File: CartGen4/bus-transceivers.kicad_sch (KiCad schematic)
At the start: 5 parts

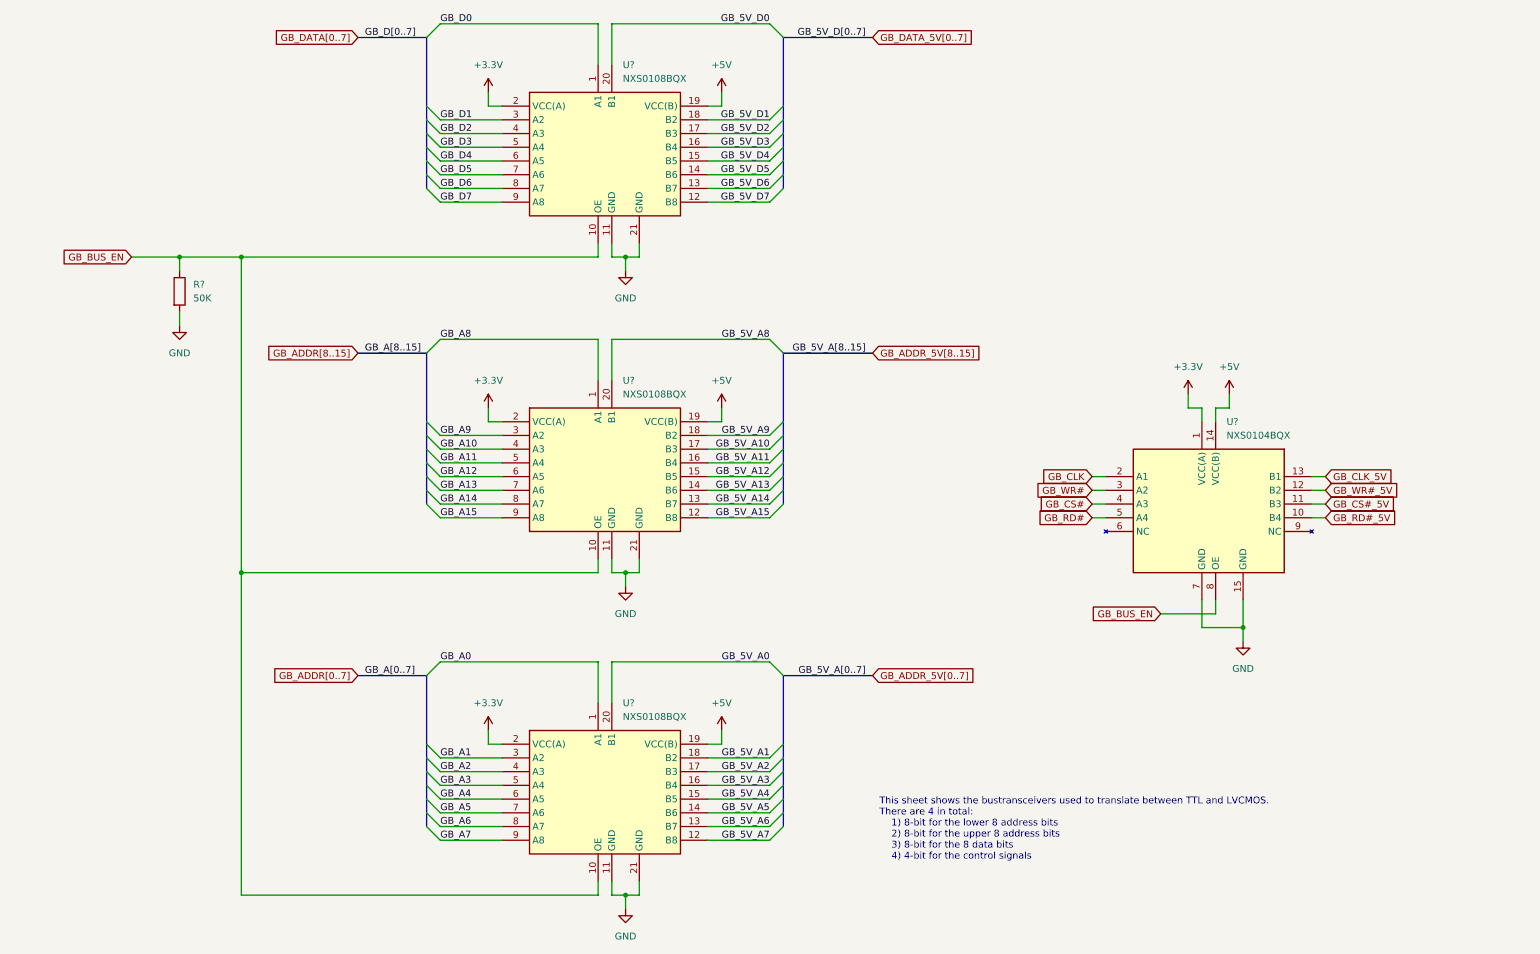
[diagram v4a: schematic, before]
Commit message: Added reference designators to everything
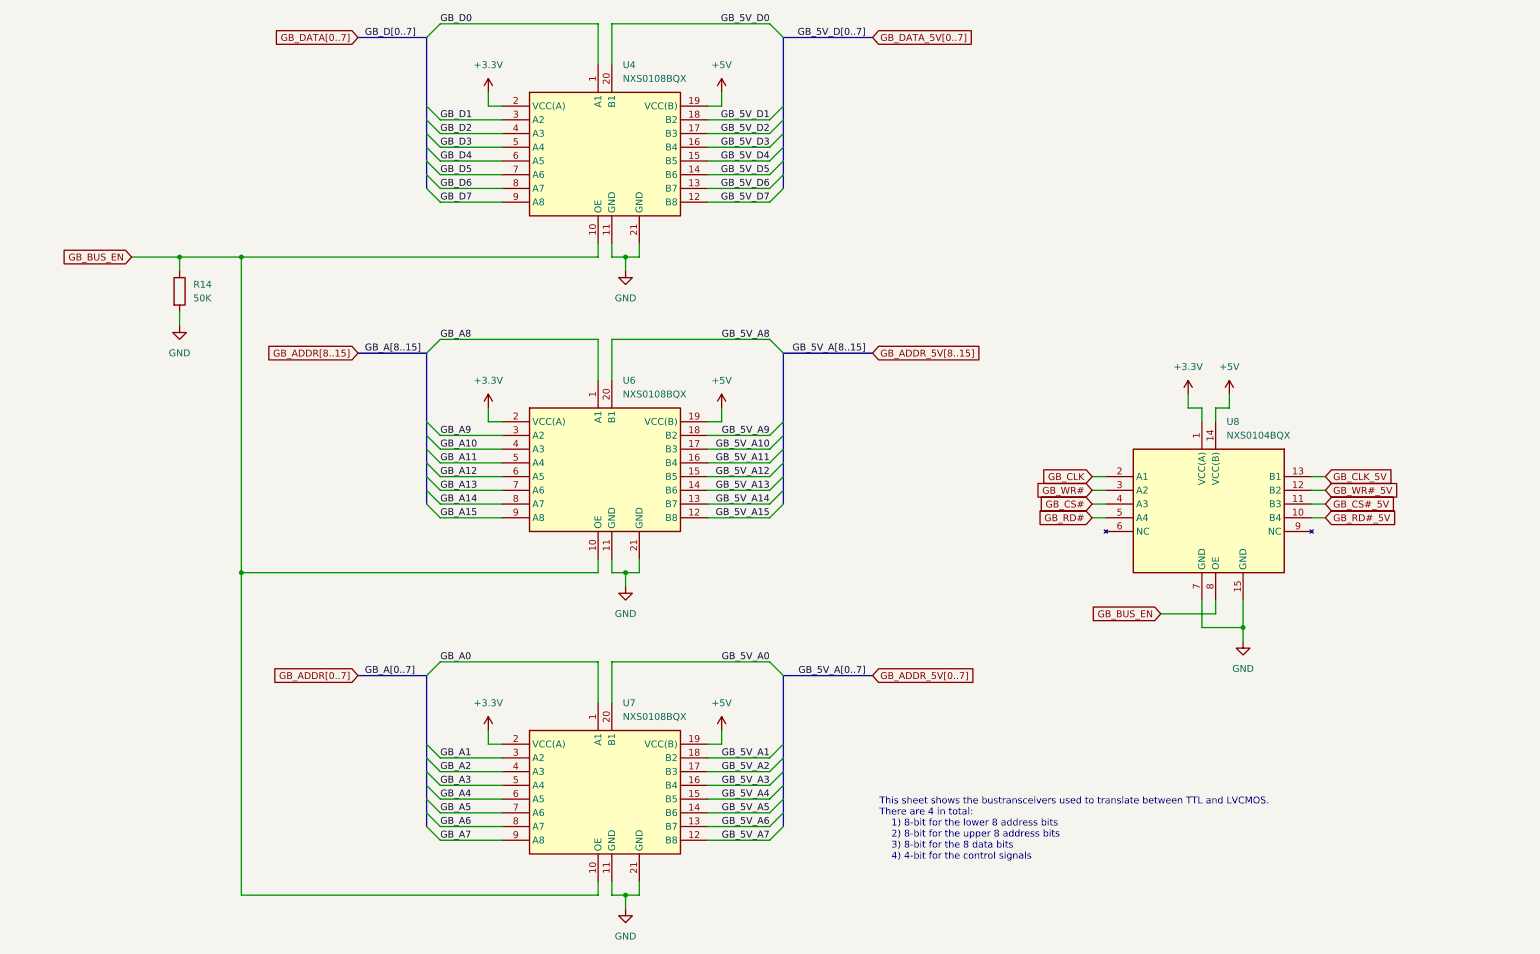
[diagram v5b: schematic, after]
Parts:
- gave numbers to parts that had none: 5
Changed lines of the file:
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@@
   (symbol (lib_id "power:GND") (at 246.38 138.43 0) (unit 1)
     (in_bom yes) (on_board yes)
-    (property "Reference" "#PWR?" (id 0) (at 246.38 144.78 0)
+    (property "Reference" "#PWR056" (id 0) (at 246.38 144.78 0)
       (effects (font (size 1.27 1.27)) hide)
     )
@@
   (symbol (lib_id "power:+5V") (at 149.86 95.25 0) (unit 1)
     (in_bom yes) (on_board yes) (fields_autoplaced)
-    (property "Reference" "#PWR?" (id 0) (at 149.86 99.06 0)
+    (property "Reference" "#PWR052" (id 0) (at 149.86 99.06 0)
       (effects (font (size 1.27 1.27)) hide)
     )
@@
   (symbol (lib_id "power:GND") (at 132.08 69.85 0) (unit 1)
     (in_bom yes) (on_board yes) (fields_autoplaced)
-    (property "Reference" "#PWR?" (id 0) (at 132.08 76.2 0)
+    (property "Reference" "#PWR042" (id 0) (at 132.08 76.2 0)
       (effects (font (size 1.27 1.27)) hide)
     )
@@
   (symbol (lib_id "SamacSys_Parts:NXS0108BQX") (at 114.3 95.25 0) (unit 1)
     (in_bom yes) (on_board yes) (fields_autoplaced)
-    (property "Reference" "U?" (id 0) (at 131.5594 90.17 0)
+    (property "Reference" "U6" (id 0) (at 131.5594 90.17 0)
       (effects (font (size 1.27 1.27)) (justify left))
     )
@@
   (symbol (lib_id "power:+5V") (at 149.86 154.94 0) (unit 1)
     (in_bom yes) (on_board yes) (fields_autoplaced)
-    (property "Reference" "#PWR?" (id 0) (at 149.86 158.75 0)
+    (property "Reference" "#PWR053" (id 0) (at 149.86 158.75 0)
       (effects (font (size 1.27 1.27)) hide)
     )
@@
   (symbol (lib_id "power:GND") (at 132.08 128.27 0) (unit 1)
     (in_bom yes) (on_board yes) (fields_autoplaced)
-    (property "Reference" "#PWR?" (id 0) (at 132.08 134.62 0)
+    (property "Reference" "#PWR043" (id 0) (at 132.08 134.62 0)
       (effects (font (size 1.27 1.27)) hide)
     )
@@
   (symbol (lib_id "power:+5V") (at 149.86 36.83 0) (unit 1)
     (in_bom yes) (on_board yes) (fields_autoplaced)
-    (property "Reference" "#PWR?" (id 0) (at 149.86 40.64 0)
+    (property "Reference" "#PWR051" (id 0) (at 149.86 40.64 0)
       (effects (font (size 1.27 1.27)) hide)
     )
@@
   (symbol (lib_id "power:GND") (at 49.53 80.01 0) (unit 1)
     (in_bom yes) (on_board yes) (fields_autoplaced)
-    (property "Reference" "#PWR?" (id 0) (at 49.53 86.36 0)
+    (property "Reference" "#PWR038" (id 0) (at 49.53 86.36 0)
       (effects (font (size 1.27 1.27)) hide)
     )
@@
   (symbol (lib_id "power:+3.3V") (at 106.68 36.83 0) (unit 1)
     (in_bom yes) (on_board yes) (fields_autoplaced)
-    (property "Reference" "#PWR?" (id 0) (at 106.68 40.64 0)
+    (property "Reference" "#PWR039" (id 0) (at 106.68 40.64 0)
       (effects (font (size 1.27 1.27)) hide)
     )
@@
   (symbol (lib_id "power:+5V") (at 243.84 92.71 0) (unit 1)
     (in_bom yes) (on_board yes) (fields_autoplaced)
-    (property "Reference" "#PWR?" (id 0) (at 243.84 96.52 0)
+    (property "Reference" "#PWR055" (id 0) (at 243.84 96.52 0)
       (effects (font (size 1.27 1.27)) hide)
     )
@@
   (symbol (lib_id "Device:R") (at 49.53 73.66 0) (unit 1)
     (in_bom yes) (on_board yes) (fields_autoplaced)
-    (property "Reference" "R?" (id 0) (at 52.07 72.3899 0)
+    (property "Reference" "R14" (id 0) (at 52.07 72.3899 0)
       (effects (font (size 1.27 1.27)) (justify left))
     )
@@
   (symbol (lib_id "SamacSys_Parts:NXS0108BQX") (at 114.3 154.94 0) (unit 1)
     (in_bom yes) (on_board yes) (fields_autoplaced)
-    (property "Reference" "U?" (id 0) (at 131.5594 149.86 0)
+    (property "Reference" "U7" (id 0) (at 131.5594 149.86 0)
       (effects (font (size 1.27 1.27)) (justify left))
     )
@@
   (symbol (lib_id "SamacSys_Parts:NXS0108BQX") (at 114.3 36.83 0) (unit 1)
     (in_bom yes) (on_board yes) (fields_autoplaced)
-    (property "Reference" "U?" (id 0) (at 131.5594 31.75 0)
+    (property "Reference" "U4" (id 0) (at 131.5594 31.75 0)
       (effects (font (size 1.27 1.27)) (justify left))
     )
@@
   (symbol (lib_id "power:+3.3V") (at 106.68 95.25 0) (unit 1)
     (in_bom yes) (on_board yes) (fields_autoplaced)
-    (property "Reference" "#PWR?" (id 0) (at 106.68 99.06 0)
+    (property "Reference" "#PWR040" (id 0) (at 106.68 99.06 0)
       (effects (font (size 1.27 1.27)) hide)
     )
@@
   (symbol (lib_id "power:+3.3V") (at 236.22 92.71 0) (unit 1)
     (in_bom yes) (on_board yes) (fields_autoplaced)
-    (property "Reference" "#PWR?" (id 0) (at 236.22 96.52 0)
+    (property "Reference" "#PWR054" (id 0) (at 236.22 96.52 0)
       (effects (font (size 1.27 1.27)) hide)
     )
@@
   (symbol (lib_id "power:+3.3V") (at 106.68 154.94 0) (unit 1)
     (in_bom yes) (on_board yes) (fields_autoplaced)
-    (property "Reference" "#PWR?" (id 0) (at 106.68 158.75 0)
+    (property "Reference" "#PWR041" (id 0) (at 106.68 158.75 0)
       (effects (font (size 1.27 1.27)) hide)
     )
@@
   (symbol (lib_id "power:GND") (at 132.08 187.96 0) (unit 1)
     (in_bom yes) (on_board yes) (fields_autoplaced)
-    (property "Reference" "#PWR?" (id 0) (at 132.08 194.31 0)
+    (property "Reference" "#PWR050" (id 0) (at 132.08 194.31 0)
       (effects (font (size 1.27 1.27)) hide)
     )
@@
   (symbol (lib_id "SamacSys_Parts:NXS0104BQX") (at 226.06 102.87 0) (unit 1)
     (in_bom yes) (on_board yes) (fields_autoplaced)
-    (property "Reference" "U?" (id 0) (at 243.3194 97.79 0)
-      (effects (font (size 1.27 1.27)) (justify left))
-    )
+    (property "Reference" "U8" (id 0) (at 243.3194 97.79 0)
+      (effects (font (size 1.27 1.27)) (justify left))
+    )

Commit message: Cleaned up symbol fields
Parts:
- U4, U6, U7: Datasheet_1 https://assets.nexperia.com/documents/data-sheet/NXS0108.pdf -> (none); Footprint_1 NXS0108BQX -> (none); Height 1 -> (none); MFN (none) -> Nexperia; MFP (none) -> NXS0108BQX; Manufacturer_Name Nexperia -> (none); Manufacturer_Part_Number NXS0108BQX -> (none); Mouser Part Number 771-NXS0108BQX -> (none); Mouser Price/Stock https://www.mouser.co.uk/ProductDetail/Nexperia/NXS0108BQX?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 -> (none)
- U8: Height 1 -> (none); MFN (none) -> Nexperia; MFP (none) -> NXS0104BQX; Manufacturer_Name Nexperia -> (none); Manufacturer_Part_Number NXS0104BQX -> (none); Mouser Part Number 771-NXS0104BQX -> (none); Mouser Price/Stock https://www.mouser.co.uk/ProductDetail/Nexperia/NXS0104BQX?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 -> (none)
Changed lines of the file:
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@@
       (effects (font (size 1.27 1.27)) hide)
     )
-    (property "Datasheet" "" (id 3) (at 129.54 90.17 90)
-      (effects (font (size 1.27 1.27)) hide)
-    )
-    (property "Footprint_1" "NXS0108BQX" (id 4) (at 157.48 83.82 0)
-      (effects (font (size 1.27 1.27)) (justify left top) hide)
-    )
-    (property "Datasheet_1" "https://assets.nexperia.com/documents/data-sheet/NXS0108.pdf" (id 5) (at 142.24 291.44 0)
-      (effects (font (size 1.27 1.27)) (justify left top) hide)
-    )
-    (property "Height" "1" (id 6) (at 142.24 491.44 0)
-      (effects (font (size 1.27 1.27)) (justify left top) hide)
-    )
-    (property "Mouser Part Number" "771-NXS0108BQX" (id 7) (at 142.24 591.44 0)
-      (effects (font (size 1.27 1.27)) (justify left top) hide)
-    )
-    (property "Mouser Price/Stock" "https://www.mouser.co.uk/ProductDetail/Nexperia/NXS0108BQX?qs=zW32dvEIR3sbMzR%252BjRaycw%3D%3D" (id 8) (at 142.24 691.44 0)
-      (effects (font (size 1.27 1.27)) (justify left top) hide)
-    )
-    (property "Manufacturer_Name" "Nexperia" (id 9) (at 142.24 791.44 0)
-      (effects (font (size 1.27 1.27)) (justify left top) hide)
-    )
-    (property "Manufacturer_Part_Number" "NXS0108BQX" (id 10) (at 142.24 891.44 0)
+    (property "Datasheet" "https://eu.mouser.com/datasheet/2/916/NXS0108-1919490.pdf" (id 3) (at 129.54 90.17 90)
+      (effects (font (size 1.27 1.27)) hide)
+    )
+    (property "MFN" "Nexperia" (id 4) (at 142.24 791.44 0)
+      (effects (font (size 1.27 1.27)) (justify left top) hide)
+    )
+    (property "MFP" "NXS0108BQX" (id 5) (at 142.24 891.44 0)
       (effects (font (size 1.27 1.27)) (justify left top) hide)
     )
@@
     (pin "2")
   )
-  (symbol (lib_id "SamacSys_Parts:NXS0108BQX") (at 114.3 154.94 0) (unit 1)
+  (symbol (lib_name "NXS0108BQX_1") (lib_id "SamacSys_Parts:NXS0108BQX") (at 114.3 154.94 0) (unit 1)
     (in_bom yes) (on_board yes) (fields_autoplaced)
     (property "Reference" "U7" (id 0) (at 131.5594 149.86 0)
@@
       (effects (font (size 1.27 1.27)) hide)
     )
-    (property "Datasheet" "" (id 3) (at 129.54 149.86 90)
-      (effects (font (size 1.27 1.27)) hide)
-    )
-    (property "Footprint_1" "NXS0108BQX" (id 4) (at 157.48 143.51 0)
-      (effects (font (size 1.27 1.27)) (justify left top) hide)
-    )
-    (property "Datasheet_1" "https://assets.nexperia.com/documents/data-sheet/NXS0108.pdf" (id 5) (at 142.24 351.13 0)
-      (effects (font (size 1.27 1.27)) (justify left top) hide)
-    )
-    (property "Height" "1" (id 6) (at 142.24 551.13 0)
-      (effects (font (size 1.27 1.27)) (justify left top) hide)
-    )
-    (property "Mouser Part Number" "771-NXS0108BQX" (id 7) (at 142.24 651.13 0)
-      (effects (font (size 1.27 1.27)) (justify left top) hide)
-    )
-    (property "Mouser Price/Stock" "https://www.mouser.co.uk/ProductDetail/Nexperia/NXS0108BQX?qs=zW32dvEIR3sbMzR%252BjRaycw%3D%3D" (id 8) (at 142.24 751.13 0)
-      (effects (font (size 1.27 1.27)) (justify left top) hide)
-    )
-    (property "Manufacturer_Name" "Nexperia" (id 9) (at 142.24 851.13 0)
-      (effects (font (size 1.27 1.27)) (justify left top) hide)
-    )
-    (property "Manufacturer_Part_Number" "NXS0108BQX" (id 10) (at 142.24 951.13 0)
+    (property "Datasheet" "https://eu.mouser.com/datasheet/2/916/NXS0108-1919490.pdf" (id 3) (at 129.54 149.86 90)
+      (effects (font (size 1.27 1.27)) hide)
+    )
+    (property "MFN" "Nexperia" (id 4) (at 142.24 851.13 0)
+      (effects (font (size 1.27 1.27)) (justify left top) hide)
+    )
+    (property "MFP" "NXS0108BQX" (id 5) (at 142.24 951.13 0)
       (effects (font (size 1.27 1.27)) (justify left top) hide)
     )
@@
     (pin "9")
   )
-  (symbol (lib_id "SamacSys_Parts:NXS0108BQX") (at 114.3 36.83 0) (unit 1)
+  (symbol (lib_name "NXS0108BQX_2") (lib_id "SamacSys_Parts:NXS0108BQX") (at 114.3 36.83 0) (unit 1)
     (in_bom yes) (on_board yes) (fields_autoplaced)
     (property "Reference" "U4" (id 0) (at 131.5594 31.75 0)
@@
       (effects (font (size 1.27 1.27)) hide)
     )
-    (property "Datasheet" "" (id 3) (at 129.54 31.75 90)
-      (effects (font (size 1.27 1.27)) hide)
-    )
-    (property "Footprint_1" "NXS0108BQX" (id 4) (at 157.48 25.4 0)
-      (effects (font (size 1.27 1.27)) (justify left top) hide)
-    )
-    (property "Datasheet_1" "https://assets.nexperia.com/documents/data-sheet/NXS0108.pdf" (id 5) (at 142.24 233.02 0)
-      (effects (font (size 1.27 1.27)) (justify left top) hide)
-    )
-    (property "Height" "1" (id 6) (at 142.24 433.02 0)
-      (effects (font (size 1.27 1.27)) (justify left top) hide)
-    )
-    (property "Mouser Part Number" "771-NXS0108BQX" (id 7) (at 142.24 533.02 0)
-      (effects (font (size 1.27 1.27)) (justify left top) hide)
-    )
-    (property "Mouser Price/Stock" "https://www.mouser.co.uk/ProductDetail/Nexperia/NXS0108BQX?qs=zW32dvEIR3sbMzR%252BjRaycw%3D%3D" (id 8) (at 142.24 633.02 0)
-      (effects (font (size 1.27 1.27)) (justify left top) hide)
-    )
-    (property "Manufacturer_Name" "Nexperia" (id 9) (at 142.24 733.02 0)
-      (effects (font (size 1.27 1.27)) (justify left top) hide)
-    )
-    (property "Manufacturer_Part_Number" "NXS0108BQX" (id 10) (at 142.24 833.02 0)
+    (property "Datasheet" "https://eu.mouser.com/datasheet/2/916/NXS0108-1919490.pdf" (id 3) (at 129.54 31.75 90)
+      (effects (font (size 1.27 1.27)) hide)
+    )
+    (property "MFN" "Nexperia" (id 9) (at 142.24 733.02 0)
+      (effects (font (size 1.27 1.27)) (justify left top) hide)
+    )
+    (property "MFP" "NXS0108BQX" (id 10) (at 142.24 833.02 0)
       (effects (font (size 1.27 1.27)) (justify left top) hide)
     )
@@
       (effects (font (size 1.27 1.27)) hide)
     )
-    (property "Height" "1" (id 4) (at 252.73 497.79 0)
-      (effects (font (size 1.27 1.27)) (justify left top) hide)
-    )
-    (property "Mouser Part Number" "771-NXS0104BQX" (id 5) (at 252.73 597.79 0)
-      (effects (font (size 1.27 1.27)) (justify left top) hide)
-    )
-    (property "Mouser Price/Stock" "https://www.mouser.co.uk/ProductDetail/Nexperia/NXS0104BQX?qs=2WXlatMagcEya%2F7vq6wExg%3D%3D" (id 6) (at 252.73 697.79 0)
-      (effects (font (size 1.27 1.27)) (justify left top) hide)
-    )
-    (property "Manufacturer_Name" "Nexperia" (id 7) (at 252.73 797.79 0)
-      (effects (font (size 1.27 1.27)) (justify left top) hide)
-    )
-    (property "Manufacturer_Part_Number" "NXS0104BQX" (id 8) (at 252.73 897.79 0)
-      (effects (font (size 1.27 1.27)) (justify left top) hide)
-    )
+    (property "MFN" "Nexperia" (id 4) (at 252.73 797.79 0)
+      (effects (font (size 1.27 1.27)) (justify left top) hide)
+    )
+    (property "MFP" "NXS0104BQX" (id 5) (at 252.73 897.79 0)
+      (effects (font (size 1.27 1.27)) (justify left top) hide)
+    )

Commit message: Added symbol information to obvious stuff
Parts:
- U4, U6, U7: Critical (none) -> Y; Notes (none) -> Used for voltage conversion between FPGA and Gameboy addres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; Package ID (none) -> DHVQFN-20; Source (none) -> SPEC
- U8: Critical (none) -> Y; Notes (none) -> Used for voltage conversion between FPGA and Gameboy contro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; Package ID (none) -> DHVQFN-14; Source (none) -> SPEC
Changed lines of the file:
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@@
       (effects (font (size 1.27 1.27)) (justify left top) hide)
+    )
+    (property "Description" "8-bit Bidirectional Voltage Translator" (id 6) (at 114.3 95.25 0)
+      (effects (font (size 1.27 1.27)) hide)
+    )
+    (property "Notes" "Used for voltage conversion between FPGA and Gameboy addres and data signals." (id 7) (at 114.3 95.25 0)
+      (effects (font (size 1.27 1.27)) hide)
+    )
+    (property "Package ID" "DHVQFN-20" (id 8) (at 114.3 95.25 0)
+      (effects (font (size 1.27 1.27)) hide)
+    )
+    (property "Source" "SPEC" (id 9) (at 114.3 95.25 0)
+      (effects (font (size 1.27 1.27)) hide)
+    )
+    (property "Critical" "Y" (id 10) (at 114.3 95.25 0)
+      (effects (font (size 1.27 1.27)) hide)
     )
     (pin "1")
@@
       (effects (font (size 1.27 1.27)) (justify left top) hide)
     )
+    (property "Description" "8-bit Bidirectional Voltage Translator" (id 6) (at 114.3 154.94 0)
+      (effects (font (size 1.27 1.27)) hide)
+    )
+    (property "Notes" "Used for voltage conversion between FPGA and Gameboy addres and data signals." (id 7) (at 114.3 154.94 0)
+      (effects (font (size 1.27 1.27)) hide)
+    )
+    (property "Package ID" "DHVQFN-20" (id 8) (at 114.3 154.94 0)
+      (effects (font (size 1.27 1.27)) hide)
+    )
+    (property "Source" "SPEC" (id 9) (at 114.3 154.94 0)
+      (effects (font (size 1.27 1.27)) hide)
+    )
+    (property "Critical" "Y" (id 10) (at 114.3 154.94 0)
+      (effects (font (size 1.27 1.27)) hide)
+    )
     (pin "1")
     (pin "10")
@@
       (effects (font (size 1.27 1.27)) (justify left top) hide)
     )
+    (property "Description" "8-bit Bidirectional Voltage Translator" (id 11) (at 114.3 36.83 0)
+      (effects (font (size 1.27 1.27)) hide)
+    )
+    (property "Notes" "Used for voltage conversion between FPGA and Gameboy addres and data signals." (id 12) (at 114.3 36.83 0)
+      (effects (font (size 1.27 1.27)) hide)
+    )
+    (property "Package ID" "DHVQFN-20" (id 13) (at 114.3 36.83 0)
+      (effects (font (size 1.27 1.27)) hide)
+    )
+    (property "Source" "SPEC" (id 14) (at 114.3 36.83 0)
+      (effects (font (size 1.27 1.27)) hide)
+    )
+    (property "Critical" "Y" (id 15) (at 114.3 36.83 0)
+      (effects (font (size 1.27 1.27)) hide)
+    )
     (pin "1")
     (pin "10")
@@
       (effects (font (size 1.27 1.27)) (justify left top) hide)
     )
-    (pin "1")
+    (property "Description" "4-bit Bidirectional Voltage Translator" (id 6) (at 226.06 102.87 0)
+      (effects (font (size 1.27 1.27)) hide)
+    )
+    (property "Notes" "Used for voltage conversion between FPGA and Gameboy control signals." (id 7) (at 226.06 102.87 0)
+      (effects (font (size 1.27 1.27)) hide)
+    )
+    (property "Package ID" "DHVQFN-14" (id 8) (at 226.06 102.87 0)
+      (effects (font (size 1.27 1.27)) hide)
+    )
+    (property "Source" "SPEC" (id 9) (at 226.06 102.87 0)
+      (effects (font (size 1.27 1.27)) hide)
+    )
+    (property "Critical" "Y" (id 10) (at 226.06 102.87 0)
+      (effects (font (size 1.27 1.27)) hide)
+    )
+    (pin "1")
